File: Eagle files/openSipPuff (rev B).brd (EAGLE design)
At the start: 30.1 x 58.7 mm, 20 parts, among them J2 1X04-RA, J3 AVR_SPI_PRG_62X3_LOCK, U1 ATMEGA32U4TQFP, U2 AD8223, U3 MPX12GP, Y1 16MHz

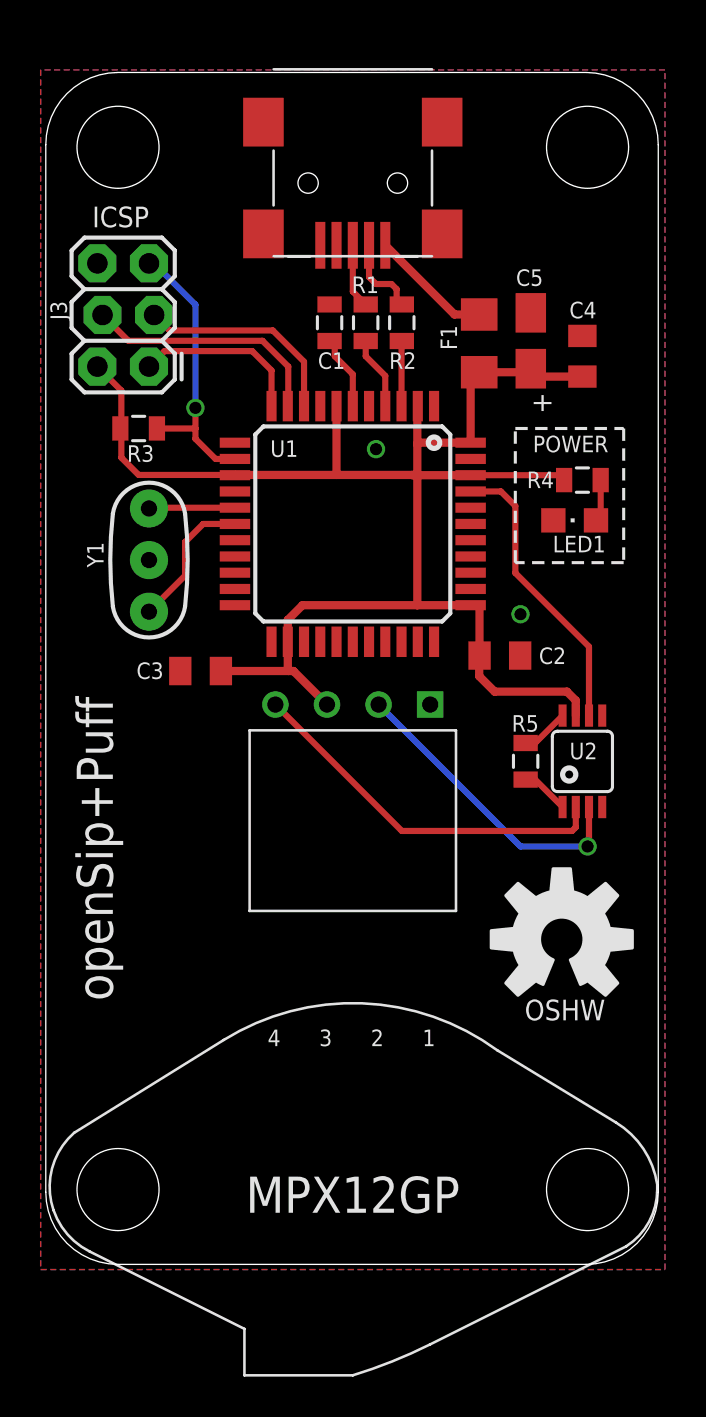
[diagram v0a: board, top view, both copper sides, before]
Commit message: Firmware update and rev B Eagle files
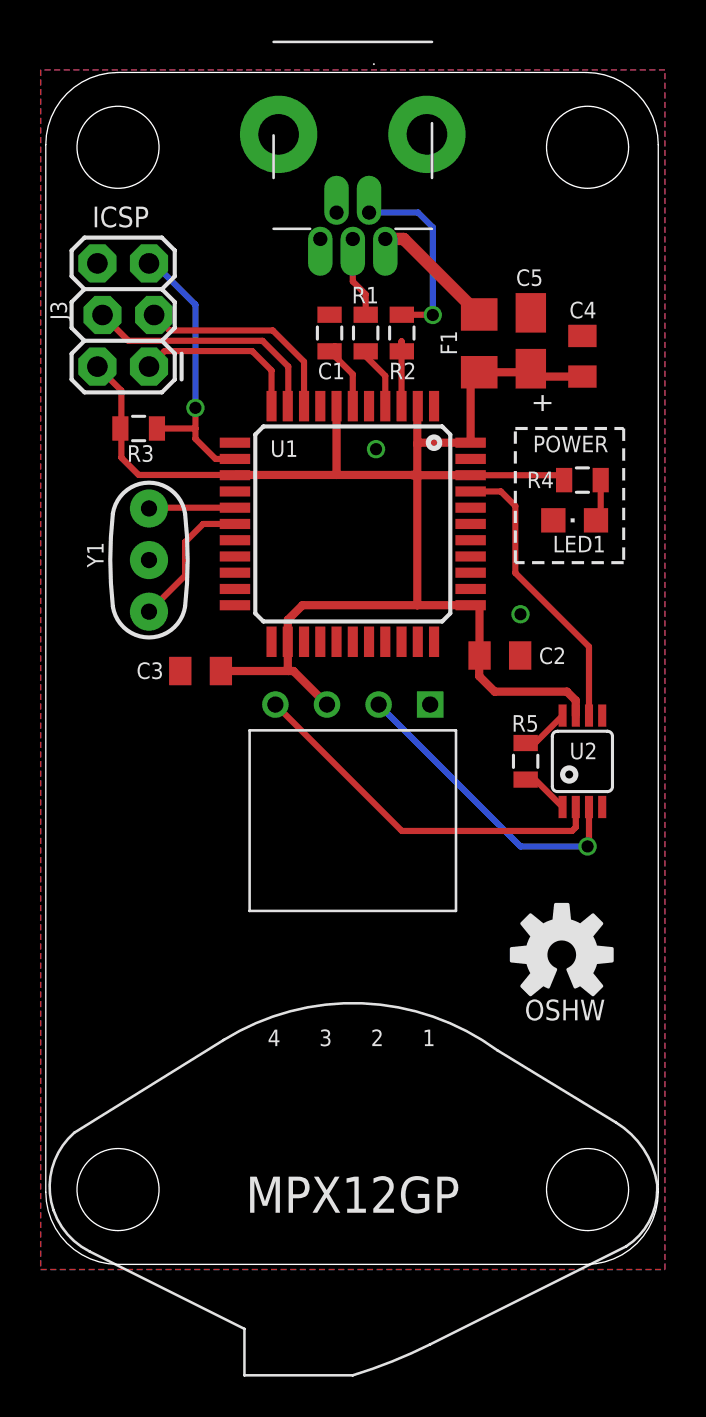
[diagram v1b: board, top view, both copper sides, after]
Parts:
- removed J1: (no value), adafruit:USB-MINIB
- added CN1: (no value), adafruit:USB-MINIB-THM-MOLEX
- C1: value 0.1uF -> 1uF
- LOGO1: value OSHW-LOGOL -> OSHW-LOGOM; device SparkFun-Aesthetics:OSHW-LOGO-L -> SparkFun-Aesthetics:OSHW-LOGO-M
- R5: value 2.4k -> 1.3k
- moved LOGO1 0.76 mm to (25.4, 15.2)
- moved C1 0.51 mm to (14.0, 45.8)
- moved R1 0.51 mm to (15.7, 45.8)
- moved R2 0.51 mm to (17.5, 45.8)
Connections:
- net OUTPUT renamed SENSOR_OUT
- removed net N$8: J1.D+, R1.1
- removed net N$9: J1.D-, R2.1
- new net D+: CN1.D+, R1.1
- new net D-: CN1.D-, R2.1
- net GND: now also CN1.GND; no longer J1.GND
- net N$4: now also CN1.VBUS; no longer J1.VBUS
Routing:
- net D-: track 0.00 -> 9.28 mm, vias 0 -> 1
- net N$9: track 4.02 -> 0.00 mm
- net D+: track 0.00 -> 3.99 mm
- net N$8: track 3.17 -> 0.00 mm
- net N$1: track 3.61 -> 3.10 mm
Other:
- board text added: "rev B"
